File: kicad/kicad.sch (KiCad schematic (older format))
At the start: 10 parts, among them J1 USB_A_MALE, U1 LD1117S33TR_SOT223, U2 ADA4807-2ARM

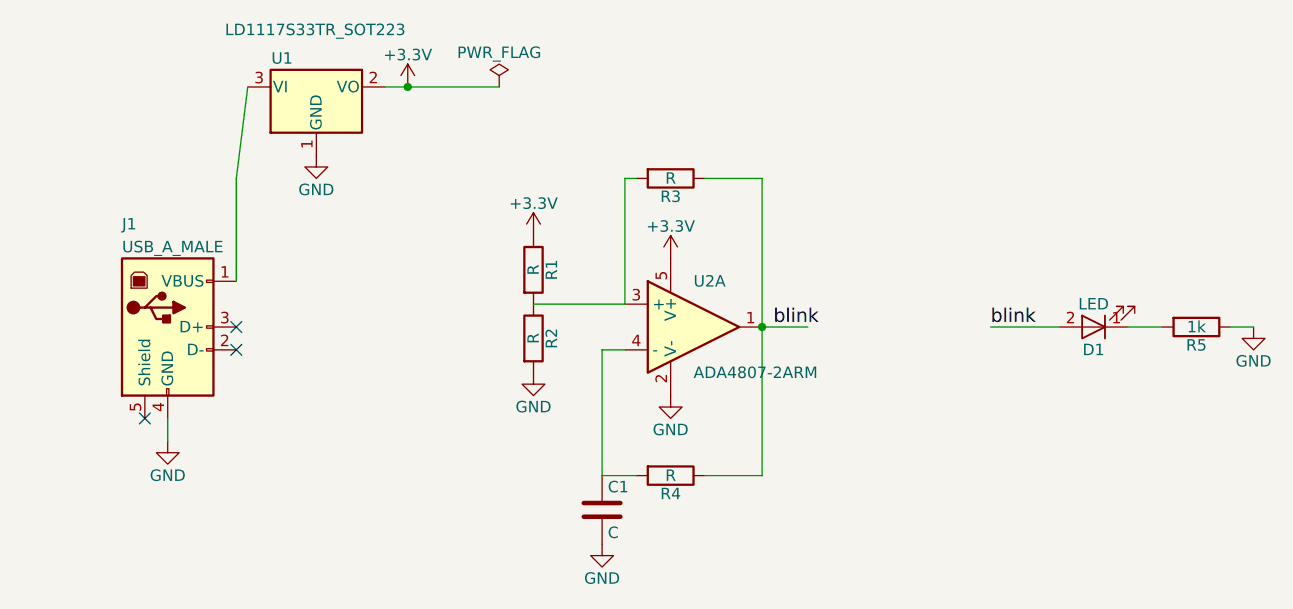
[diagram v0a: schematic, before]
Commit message: Added bypass caps
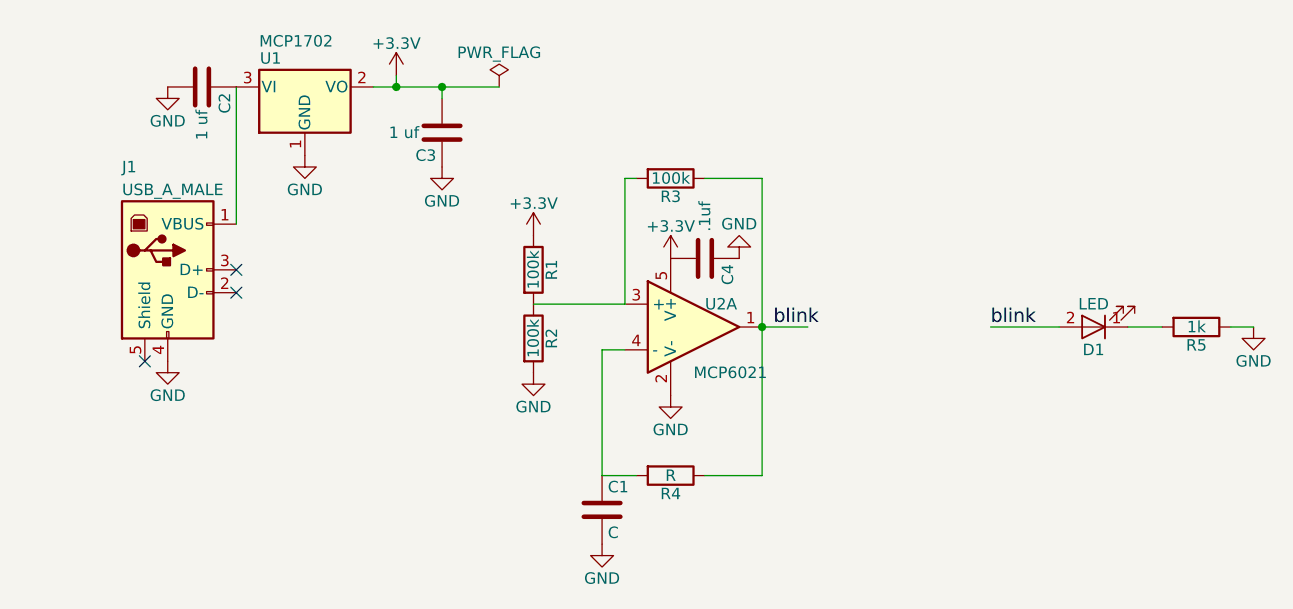
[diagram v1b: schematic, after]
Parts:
- added C2, C3: 1 uf, Capacitors_SMD:C_0603, symbol C
- added C4: .1uf, Capacitors_SMD:C_0603, symbol C
- J1: footprint (none) -> Connectors:USB_A
- R1, R2, R3: value R -> 100k
- U1: value LD1117S33TR_SOT223 -> MCP1702; footprint TO_SOT_Packages_SMD:SOT-223-3Lead_TabPin2 -> TO_SOT_Packages_SMD:SOT-23
- U2: value ADA4807-2ARM -> MCP6021; footprint Housings_CSP:LFCSP-8_2x2mm_Pitch0.5mm -> TO_SOT_Packages_SMD:SOT-23-5
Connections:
- wire segments 20 -> 19
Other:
- moved on the sheet: J1, U1
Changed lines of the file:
@@
 U 1 1 59ADC200
 P 3800 3800
-F 0 "U2" H 3800 4000 50  0000 L CNN
-F 1 "ADA4807-2ARM" H 3800 3600 50  0000 L CNN
-F 2 "Housings_CSP:LFCSP-8_2x2mm_Pitch0.5mm" H 3800 3800 50  0001 C CNN
+F 0 "U2" H 3850 3900 50  0000 L CNN
+F 1 "MCP6021" H 3800 3600 50  0000 L CNN
+F 2 "TO_SOT_Packages_SMD:SOT-23-5" H 3800 3800 50  0001 C CNN
 F 3 "" H 3800 3800 50  0001 C CNN
 	1    3800 3800
@@
 L LD1117S33TR_SOT223 U1
 U 1 1 59ADC255
-P 2150 2750
-F 0 "U1" H 2000 2875 50  0000 C CNN
-F 1 "LD1117S33TR_SOT223" H 1750 3000 50  0000 L CNN
-F 2 "TO_SOT_Packages_SMD:SOT-223-3Lead_TabPin2" H 2150 2950 50  0001 C CNN
-F 3 "" H 2250 2500 50  0001 C CNN
-	1    2150 2750
+P 2100 2750
+F 0 "U1" H 1950 2875 50  0000 C CNN
+F 1 "MCP1702" H 1900 2950 50  0000 L CNN
+F 2 "TO_SOT_Packages_SMD:SOT-23" H 2100 2950 50  0001 C CNN
+F 3 "" H 2200 2500 50  0001 C CNN
+	1    2100 2750
 	1    0    0    -1
 $EndComp
@@
 L +3.3V #PWR01
 U 1 1 59B71727
-P 2550 2750
-F 0 "#PWR01" H 2550 2600 50  0001 C CNN
-F 1 "+3.3V" H 2550 2890 50  0000 C CNN
-F 2 "" H 2550 2750 50  0001 C CNN
-F 3 "" H 2550 2750 50  0001 C CNN
-	1    2550 2750
+P 2500 2700
+F 0 "#PWR01" H 2500 2550 50  0001 C CNN
+F 1 "+3.3V" H 2500 2840 50  0000 C CNN
+F 2 "" H 2500 2700 50  0001 C CNN
+F 3 "" H 2500 2700 50  0001 C CNN
+	1    2500 2700
 	1    0    0    -1
 $EndComp
@@
 L GND #PWR03
 U 1 1 59B71ABA
-P 1500 4300
-F 0 "#PWR03" H 1500 4050 50  0001 C CNN
-F 1 "GND" H 1500 4150 50  0000 C CNN
-F 2 "" H 1500 4300 50  0001 C CNN
-F 3 "" H 1500 4300 50  0001 C CNN
-	1    1500 4300
+P 1500 3950
+F 0 "#PWR03" H 1500 3700 50  0001 C CNN
+F 1 "GND" H 1500 3800 50  0000 C CNN
+F 2 "" H 1500 3950 50  0001 C CNN
+F 3 "" H 1500 3950 50  0001 C CNN
+	1    1500 3950
 	1    0    0    -1
 $EndComp
@@
 L GND #PWR05
 U 1 1 59B71AFC
-P 2150 3050
-F 0 "#PWR05" H 2150 2800 50  0001 C CNN
-F 1 "GND" H 2150 2900 50  0000 C CNN
-F 2 "" H 2150 3050 50  0001 C CNN
-F 3 "" H 2150 3050 50  0001 C CNN
-	1    2150 3050
+P 2100 3050
+F 0 "#PWR05" H 2100 2800 50  0001 C CNN
+F 1 "GND" H 2100 2900 50  0000 C CNN
+F 2 "" H 2100 3050 50  0001 C CNN
+F 3 "" H 2100 3050 50  0001 C CNN
+	1    2100 3050
 	1    0    0    -1
 $EndComp
@@
 P 3700 3150
 F 0 "R3" V 3780 3150 50  0000 C CNN
-F 1 "R" V 3700 3150 50  0000 C CNN
+F 1 "100k" V 3700 3150 50  0000 C CNN
 F 2 "Resistors_SMD:R_0603" V 3630 3150 50  0001 C CNN
 F 3 "" H 3700 3150 50  0001 C CNN
@@
 P 3100 3550
 F 0 "R1" V 3180 3550 50  0000 C CNN
-F 1 "R" V 3100 3550 50  0000 C CNN
+F 1 "100k" V 3100 3550 50  0000 C CNN
 F 2 "Resistors_SMD:R_0603" V 3030 3550 50  0001 C CNN
 F 3 "" H 3100 3550 50  0001 C CNN
@@
 P 3100 3850
 F 0 "R2" V 3180 3850 50  0000 C CNN
-F 1 "R" V 3100 3850 50  0000 C CNN
+F 1 "100k" V 3100 3850 50  0000 C CNN
 F 2 "Resistors_SMD:R_0603" V 3030 3850 50  0001 C CNN
 F 3 "" H 3100 3850 50  0001 C CNN
@@
 	1    0    0    -1
 $EndComp
-NoConn ~ 1800 3800
-NoConn ~ 1800 3900
-NoConn ~ 1400 4200
+NoConn ~ 1800 3550
+NoConn ~ 1800 3650
+NoConn ~ 1400 3950
 $Comp
 L USB_A_MALE J1
 U 1 1 59B7412C
-P 1500 3800
-F 0 "J1" H 1300 4250 50  0000 L CNN
-F 1 "USB_A_MALE" H 1300 4150 50  0000 L CNN
-F 2 "" H 1650 3750 50  0001 C CNN
-F 3 "" H 1650 3750 50  0001 C CNN
-	1    1500 3800
+P 1500 3550
+F 0 "J1" H 1300 4000 50  0000 L CNN
+F 1 "USB_A_MALE" H 1300 3900 50  0000 L CNN
+F 2 "Connectors:USB_A" H 1650 3500 50  0001 C CNN
+F 3 "" H 1650 3500 50  0001 C CNN
+	1    1500 3550
 	1    0    0    -1
 $EndComp
@@
 Text Label 5100 3800 0    60   ~ 0
 blink
-Wire Wire Line
-	1800 3600 1800 3150
-Wire Wire Line
-	1800 3150 1850 2750
-Wire Wire Line
-	3700 3500 3700 3500
-Wire Wire Line
-	1500 4200 1500 4300
-Wire Wire Line
-	3700 4100 3700 4100
-Wire Wire Line
-	2150 3050 2150 3050
-Wire Wire Line
-	3550 4450 3400 4450
-Wire Wire Line
-	3400 4450 3400 3900
-Wire Wire Line
-	3400 3900 3500 3900
-Wire Wire Line
-	4100 4450 3850 4450
-Wire Wire Line
-	4100 3150 4100 4450
-Wire Wire Line
-	3850 3150 4100 3150
-Connection ~ 4100 3800
-Wire Wire Line
-	3550 3150 3500 3150
-Wire Wire Line
-	3500 3150 3500 3700
-Wire Wire Line
-	3500 3700 3100 3700
-Wire Wire Line
-	4100 3800 4300 3800
-Connection ~ 2550 2750
-Wire Wire Line
-	2450 2750 2950 2750
-Wire Wire Line
-	5100 3800 5400 3800
 $Comp
 L LED D1
@@
 	0    1    1    0
 $EndComp
-Wire Wire Line
-	5850 3800 5700 3800
-Wire Wire Line
-	6150 3800 6250 3800
 $Comp
 L GND #PWR010
@@
 	1    0    0    -1
 $EndComp
+$Comp
+L C C2
+U 1 1 59B75978
+P 1650 2750
+F 0 "C2" H 1675 2850 50  0000 L CNN
+F 1 "1 uf" H 1750 2750 50  0000 L CNN
+F 2 "Capacitors_SMD:C_0603" H 1688 2600 50  0001 C CNN
+F 3 "" H 1650 2750 50  0001 C CNN
+	1    1650 2750
+	0    1    1    0
+$EndComp
+$Comp
+L GND #PWR011
+U 1 1 59B759CA
+P 1500 2750
+F 0 "#PWR011" H 1500 2500 50  0001 C CNN
+F 1 "GND" H 1500 2600 50  0000 C CNN
+F 2 "" H 1500 2750 50  0001 C CNN
+F 3 "" H 1500 2750 50  0001 C CNN
+	1    1500 2750
+	1    0    0    -1
+$EndComp
+$Comp
+L C C3
+U 1 1 59B75B50
+P 2700 2950
+F 0 "C3" H 2725 3050 50  0000 L CNN
+F 1 "1 uf" H 2800 2950 50  0000 L CNN
+F 2 "Capacitors_SMD:C_0603" H 2738 2800 50  0001 C CNN
+F 3 "" H 2700 2950 50  0001 C CNN
+	1    2700 2950
+	-1   0    0    1
+$EndComp
+$Comp
+L GND #PWR012
+U 1 1 59B75C37
+P 2700 3100
+F 0 "#PWR012" H 2700 2850 50  0001 C CNN
+F 1 "GND" H 2700 2950 50  0000 C CNN
+F 2 "" H 2700 3100 50  0001 C CNN
+F 3 "" H 2700 3100 50  0001 C CNN
+	1    2700 3100
+	1    0    0    -1
+$EndComp
+Wire Wire Line
+	1800 2750 1800 3350
+Wire Wire Line
+	3700 3500 3700 3500
+Wire Wire Line
+	3700 4100 3700 4100
+Wire Wire Line
+	3550 4450 3400 4450
+Wire Wire Line
+	3400 4450 3400 3900
+Wire Wire Line
+	3400 3900 3500 3900
+Wire Wire Line
+	4100 4450 3850 4450
+Wire Wire Line
+	4100 3150 4100 4450
+Wire Wire Line
+	3850 3150 4100 3150
+Connection ~ 4100 3800
+Wire Wire Line
+	3550 3150 3500 3150
+Wire Wire Line
+	3500 3150 3500 3700
+Wire Wire Line
+	3500 3700 3100 3700
+Wire Wire Line
+	4100 3800 4300 3800
+Wire Wire Line
+	2400 2750 2950 2750
+Wire Wire Line
+	5100 3800 5400 3800
+Wire Wire Line
+	5850 3800 5700 3800
+Wire Wire Line
+	6150 3800 6250 3800
+Wire Wire Line
+	2700 2800 2700 2750
+Connection ~ 2700 2750
+Wire Wire Line
+	2500 2700 2500 2750
+Connection ~ 2500 2750
+$Comp
+L C C4
+U 1 1 59B7706C
+P 3850 3500
+F 0 "C4" H 3875 3600 50  0000 L CNN
+F 1 ".1uf" H 3600 3500 50  0000 L CNN
+F 2 "Capacitors_SMD:C_0603" H 3888 3350 50  0001 C CNN
+F 3 "" H 3850 3500 50  0001 C CNN
+	1    3850 3500
+	0    1    1    0
+$EndComp
+$Comp
+L GND #PWR013
+U 1 1 59B770A7
+P 4000 3500
+F 0 "#PWR013" H 4000 3250 50  0001 C CNN
+F 1 "GND" H 4000 3350 50  0000 C CNN
+F 2 "" H 4000 3500 50  0001 C CNN
+F 3 "" H 4000 3500 50  0001 C CNN
+	1    4000 3500
+	-1   0    0    1
+$EndComp
 $EndSCHEMATC

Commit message: Routed and stuff
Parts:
- removed U2: MCP6021, TO_SOT_Packages_SMD:SOT-23-5, symbol ADA4807-2ARM
- added U2: MCP6021, TO_SOT_Packages_SMD:SOT-23-5, symbol MCP6021
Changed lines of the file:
@@
 $EndDescr
-$Comp
-L ADA4807-2ARM U2
-U 1 1 59ADC200
-P 3800 3800
-F 0 "U2" H 3850 3900 50  0000 L CNN
-F 1 "MCP6021" H 3800 3600 50  0000 L CNN
-F 2 "TO_SOT_Packages_SMD:SOT-23-5" H 3800 3800 50  0001 C CNN
-F 3 "" H 3800 3800 50  0001 C CNN
-	1    3800 3800
-	1    0    0    -1
-$EndComp
 $Comp
 L LD1117S33TR_SOT223 U1
@@
 	-1   0    0    1
 $EndComp
+$Comp
+L MCP6021 U2
+U 1 1 59B72FCF
+P 3800 3800
+F 0 "U2" H 3800 4000 50  0000 L CNN
+F 1 "MCP6021" H 3800 3600 50  0000 L CNN
+F 2 "TO_SOT_Packages_SMD:SOT-23-5" H 3800 3800 50  0001 C CNN
+F 3 "" H 3800 3800 50  0001 C CNN
+	1    3800 3800
+	1    0    0    -1
+$EndComp
 $EndSCHEMATC

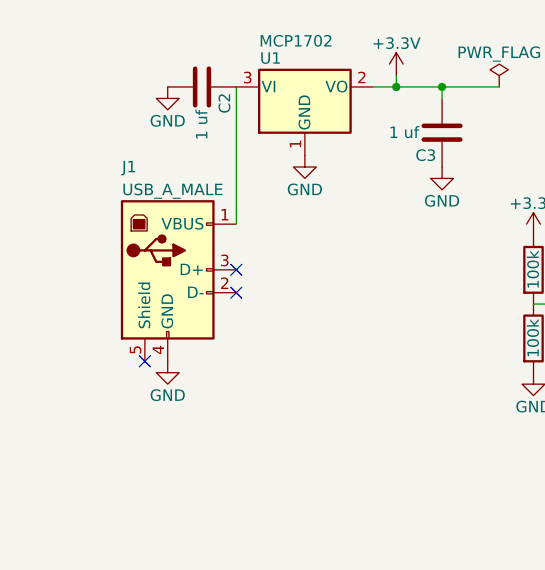
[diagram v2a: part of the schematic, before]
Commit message: Added fill of ground plane on front
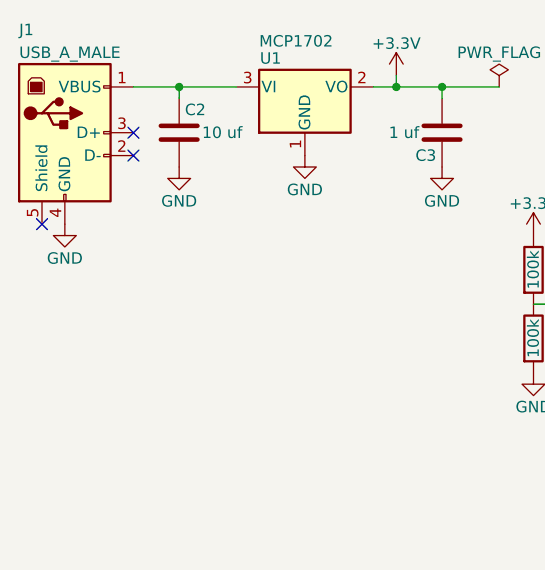
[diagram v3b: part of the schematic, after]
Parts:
- C2: value 1 uf -> 10 uf
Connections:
- wire segments 19 -> 20
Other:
- moved on the sheet: C2, J1
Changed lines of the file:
@@
 L GND #PWR03
 U 1 1 59B71ABA
-P 1500 3950
-F 0 "#PWR03" H 1500 3700 50  0001 C CNN
-F 1 "GND" H 1500 3800 50  0000 C CNN
-F 2 "" H 1500 3950 50  0001 C CNN
-F 3 "" H 1500 3950 50  0001 C CNN
-	1    1500 3950
+P 1050 3350
+F 0 "#PWR03" H 1050 3100 50  0001 C CNN
+F 1 "GND" H 1050 3200 50  0000 C CNN
+F 2 "" H 1050 3350 50  0001 C CNN
+F 3 "" H 1050 3350 50  0001 C CNN
+	1    1050 3350
 	1    0    0    -1
 $EndComp
@@
 	1    0    0    -1
 $EndComp
-NoConn ~ 1800 3550
-NoConn ~ 1800 3650
-NoConn ~ 1400 3950
+NoConn ~ 1350 2950
+NoConn ~ 1350 3050
+NoConn ~ 950  3350
 $Comp
 L USB_A_MALE J1
 U 1 1 59B7412C
-P 1500 3550
-F 0 "J1" H 1300 4000 50  0000 L CNN
-F 1 "USB_A_MALE" H 1300 3900 50  0000 L CNN
-F 2 "Connectors:USB_A" H 1650 3500 50  0001 C CNN
-F 3 "" H 1650 3500 50  0001 C CNN
-	1    1500 3550
+P 1050 2950
+F 0 "J1" H 850 3400 50  0000 L CNN
+F 1 "USB_A_MALE" H 850 3300 50  0000 L CNN
+F 2 "Connectors:USB_A" H 1200 2900 50  0001 C CNN
+F 3 "" H 1200 2900 50  0001 C CNN
+	1    1050 2950
 	1    0    0    -1
 $EndComp
@@
 L C C2
 U 1 1 59B75978
-P 1650 2750
-F 0 "C2" H 1675 2850 50  0000 L CNN
-F 1 "1 uf" H 1750 2750 50  0000 L CNN
-F 2 "Capacitors_SMD:C_0603" H 1688 2600 50  0001 C CNN
-F 3 "" H 1650 2750 50  0001 C CNN
-	1    1650 2750
-	0    1    1    0
+P 1550 2950
+F 0 "C2" H 1575 3050 50  0000 L CNN
+F 1 "10 uf" H 1650 2950 50  0000 L CNN
+F 2 "Capacitors_SMD:C_0603" H 1588 2800 50  0001 C CNN
+F 3 "" H 1550 2950 50  0001 C CNN
+	1    1550 2950
+	1    0    0    -1
 $EndComp
 $Comp
 L GND #PWR011
 U 1 1 59B759CA
-P 1500 2750
-F 0 "#PWR011" H 1500 2500 50  0001 C CNN
-F 1 "GND" H 1500 2600 50  0000 C CNN
-F 2 "" H 1500 2750 50  0001 C CNN
-F 3 "" H 1500 2750 50  0001 C CNN
-	1    1500 2750
+P 1550 3100
+F 0 "#PWR011" H 1550 2850 50  0001 C CNN
+F 1 "GND" H 1550 2950 50  0000 C CNN
+F 2 "" H 1550 3100 50  0001 C CNN
+F 3 "" H 1550 3100 50  0001 C CNN
+	1    1550 3100
 	1    0    0    -1
 $EndComp
@@
 $EndComp
 Wire Wire Line
-	1800 2750 1800 3350
+	1350 2750 1800 2750
 Wire Wire Line
 	3700 3500 3700 3500
@@
 	1    0    0    -1
 $EndComp
+Wire Wire Line
+	1550 2750 1550 2800
+Connection ~ 1550 2750
 $EndSCHEMATC

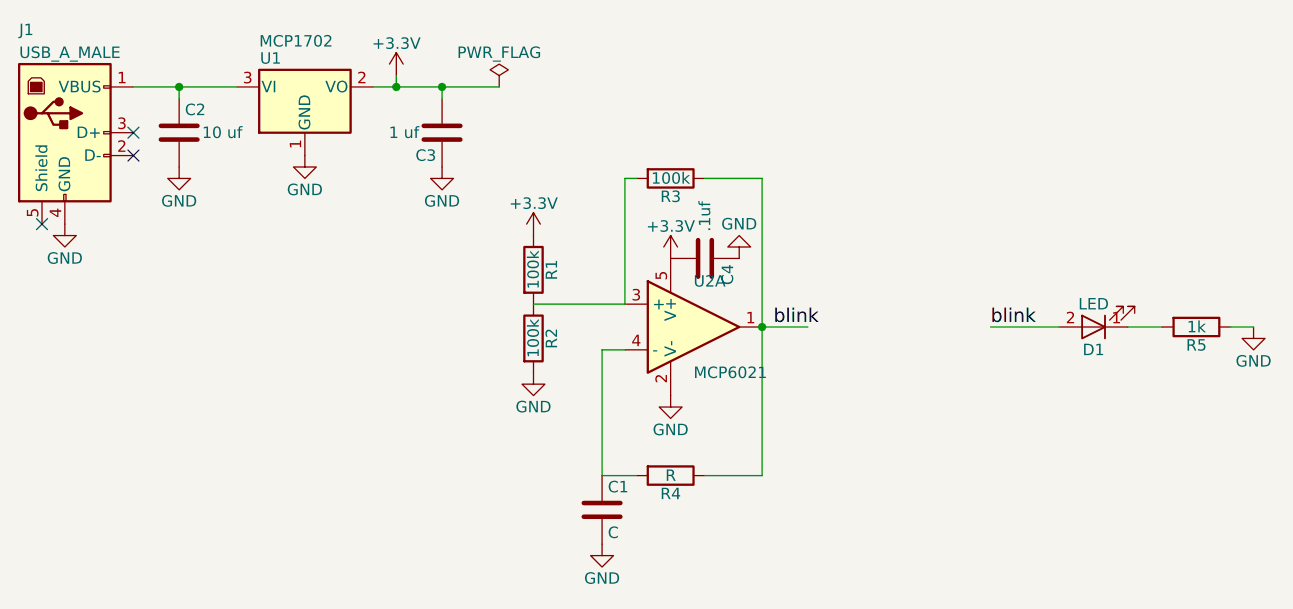
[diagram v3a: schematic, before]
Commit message: Fixed capacitor size for large caps
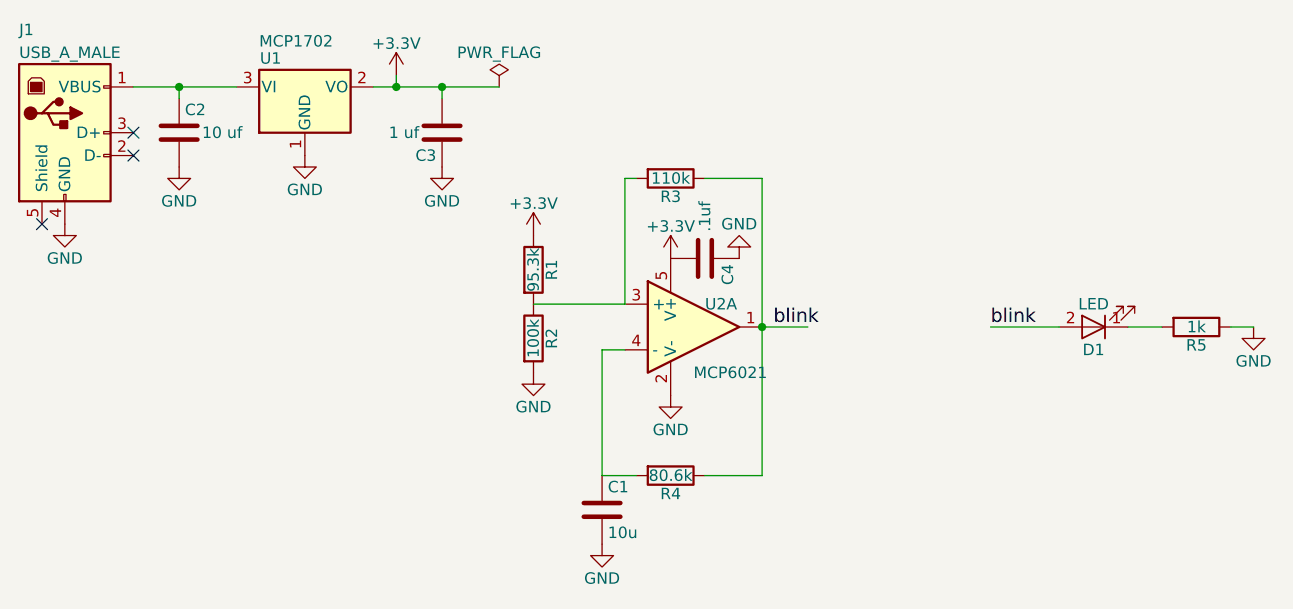
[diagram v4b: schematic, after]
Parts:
- C1: value C -> 10u
- R1: value 100k -> 95.3k
- R3: value 100k -> 110k
- R4: value R -> 80.6k
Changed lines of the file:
@@
 LIBS:valves
 LIBS:component_lib
+LIBS:pspice
 LIBS:kicad-cache
 EELAYER 25 0
@@
 P 3400 4600
 F 0 "C1" H 3425 4700 50  0000 L CNN
-F 1 "C" H 3425 4500 50  0000 L CNN
+F 1 "10u" H 3425 4500 50  0000 L CNN
 F 2 "Capacitors_SMD:C_0603" H 3438 4450 50  0001 C CNN
 F 3 "" H 3400 4600 50  0001 C CNN
@@
 P 3700 4450
 F 0 "R4" V 3780 4450 50  0000 C CNN
-F 1 "R" V 3700 4450 50  0000 C CNN
+F 1 "80.6k" V 3700 4450 50  0000 C CNN
 F 2 "Resistors_SMD:R_0603" V 3630 4450 50  0001 C CNN
 F 3 "" H 3700 4450 50  0001 C CNN
@@
 P 3700 3150
 F 0 "R3" V 3780 3150 50  0000 C CNN
-F 1 "100k" V 3700 3150 50  0000 C CNN
+F 1 "110k" V 3700 3150 50  0000 C CNN
 F 2 "Resistors_SMD:R_0603" V 3630 3150 50  0001 C CNN
 F 3 "" H 3700 3150 50  0001 C CNN
@@
 P 3100 3550
 F 0 "R1" V 3180 3550 50  0000 C CNN
-F 1 "100k" V 3100 3550 50  0000 C CNN
+F 1 "95.3k" V 3100 3550 50  0000 C CNN
 F 2 "Resistors_SMD:R_0603" V 3030 3550 50  0001 C CNN
 F 3 "" H 3100 3550 50  0001 C CNN
@@
 U 1 1 59B72FCF
 P 3800 3800
-F 0 "U2" H 3800 4000 50  0000 L CNN
+F 0 "U2" H 3850 3900 50  0000 L CNN
 F 1 "MCP6021" H 3800 3600 50  0000 L CNN
 F 2 "TO_SOT_Packages_SMD:SOT-23-5" H 3800 3800 50  0001 C CNN

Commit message: Finished board layout design for plug
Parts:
- C1, C2: footprint Capacitors_SMD:C_0603 -> Capacitors_SMD:C_0805
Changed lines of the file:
@@
 F 0 "C1" H 3425 4700 50  0000 L CNN
 F 1 "10u" H 3425 4500 50  0000 L CNN
-F 2 "Capacitors_SMD:C_0603" H 3438 4450 50  0001 C CNN
+F 2 "Capacitors_SMD:C_0805" H 3438 4450 50  0001 C CNN
 F 3 "" H 3400 4600 50  0001 C CNN
 	1    3400 4600
@@
 F 0 "C2" H 1575 3050 50  0000 L CNN
 F 1 "10 uf" H 1650 2950 50  0000 L CNN
-F 2 "Capacitors_SMD:C_0603" H 1588 2800 50  0001 C CNN
+F 2 "Capacitors_SMD:C_0805" H 1588 2800 50  0001 C CNN
 F 3 "" H 1550 2950 50  0001 C CNN
 	1    1550 2950

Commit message: Finished layout
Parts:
- C1: value 10u -> 10 uf
- J1: footprint Connectors:USB_A -> usb_male:USB_A_male
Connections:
- wire segments 20 -> 21
- no-connect marks 3 -> 2
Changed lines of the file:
@@
 P 3400 4600
 F 0 "C1" H 3425 4700 50  0000 L CNN
-F 1 "10u" H 3425 4500 50  0000 L CNN
+F 1 "10 uf" H 3425 4500 50  0000 L CNN
 F 2 "Capacitors_SMD:C_0805" H 3438 4450 50  0001 C CNN
 F 3 "" H 3400 4600 50  0001 C CNN
@@
 NoConn ~ 1350 2950
 NoConn ~ 1350 3050
-NoConn ~ 950  3350
 $Comp
 L USB_A_MALE J1
@@
 F 0 "J1" H 850 3400 50  0000 L CNN
 F 1 "USB_A_MALE" H 850 3300 50  0000 L CNN
-F 2 "Connectors:USB_A" H 1200 2900 50  0001 C CNN
+F 2 "usb_male:USB_A_male" H 1200 2900 50  0001 C CNN
 F 3 "" H 1200 2900 50  0001 C CNN
 	1    1050 2950
@@
 	1550 2750 1550 2800
 Connection ~ 1550 2750
+Wire Wire Line
+	950  3350 1050 3350
 $EndSCHEMATC
